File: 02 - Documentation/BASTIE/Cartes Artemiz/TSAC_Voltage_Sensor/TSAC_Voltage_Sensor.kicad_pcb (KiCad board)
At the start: 2 copper layers, 61 x 68.6 mm, 21 parts, among them J1 3P Droit 22-11-2032, K1 SSR CPC1394GR

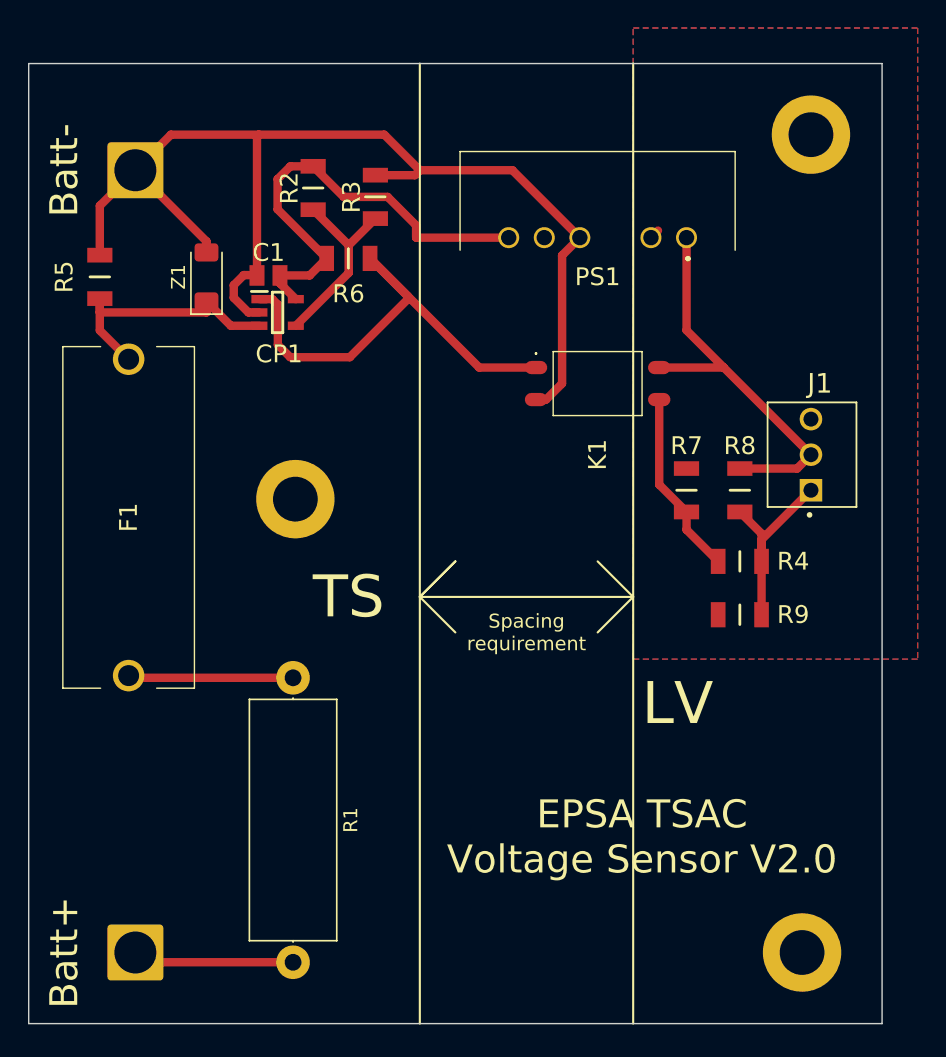
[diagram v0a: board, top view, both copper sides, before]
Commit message: Quasi fin modele 3D batterie + modif TSAC Voltage
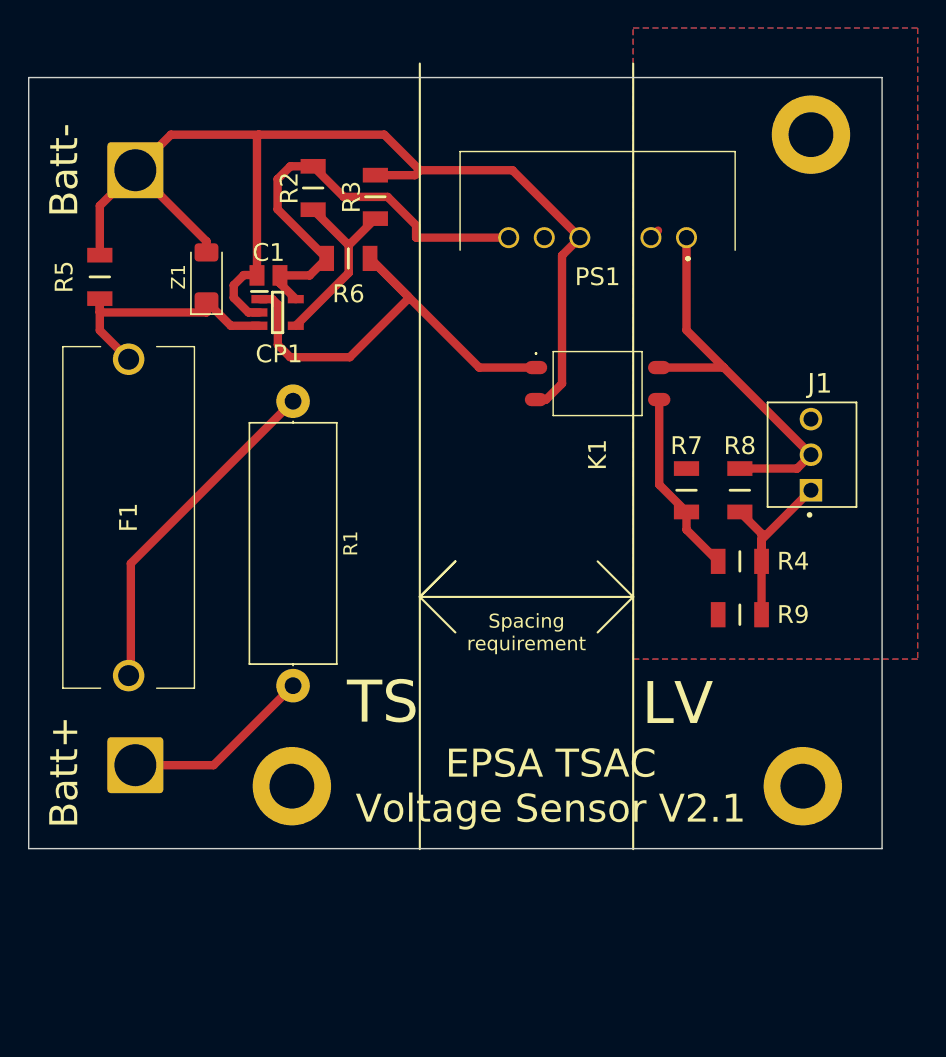
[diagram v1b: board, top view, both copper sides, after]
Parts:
- moved ? 20.5 mm to (95.0, 107.5)
- moved R1 19.8 mm to (95.1, 80.0)
- moved TP1 13.4 mm to (83.8, 106.0)
- moved ? 11.9 mm to (131.5, 107.5)
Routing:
- net Net-(F1-Pad1): track 11.6 -> 24.6 mm
- net +BATT: track 10.6 -> 13.6 mm
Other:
- board size 61 x 68.6 mm -> 61 x 55.1 mm
- board text added: "EPSA TSAC Voltage Sensor V2.1"
- board text removed: "EPSA TSAC Voltage Sensor V2.0"
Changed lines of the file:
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@@
 	(footprint ""
 		(layer "F.Cu")
-		(at 95.25 86.995)
+		(at 95 107.5)
 		(property "Reference" ""
 			(at 0 0 0)
@@
 	(footprint ""
 		(layer "F.Cu")
-		(at 131.445 119.38)
+		(at 131.5 107.5)
 		(property "Reference" ""
 			(at 0 0 0)
@@
 	(footprint "Connector_Wire:SolderWire-2.5sqmm_1x01_D2.4mm_OD3.6mm"
 		(layer "F.Cu")
-		(at 83.82 119.38)
+		(at 83.82 106)
 		(descr "Soldered wire connection, for a single 2.5 mm² wire, basic insulation, conductor diameter 2.4mm, outer diameter 3.6mm, size source Multi-Contact FLEXI-E 2.5 (https://ec.staubli.com/AcroFiles/Catalogues/TM_Cab-Main-11014119_(en)_hi.pdf), bend radius 3 times outer diameter, generated with kicad-footprint-generator")
 		(tags "connector wire 2.5sqmm")
@@
 	(footprint "Resistor_THT:R_Axial_DIN0617_L17.0mm_D6.0mm_P20.32mm_Horizontal"
 		(layer "F.Cu")
-		(at 95.085306 99.757822 -90)
+		(at 95.085306 80 -90)
 		(descr "Resistor, Axial_DIN0617 series, Axial, Horizontal, pin pitch=20.32mm, 2W, length*diameter=17*6mm^2, http://www.vishay.com/docs/20128/wkxwrx.pdf")
 		(tags "Resistor Axial_DIN0617 series Axial Horizontal pin pitch 20.32mm 2W length 17mm diameter 6mm")
 		(property "Reference" "R1"
-			(at 10.16 -4.12 -90)
+			(at 10.16 -4.12 90)
 			(layer "F.SilkS")
 			(effects
@@
 		)
 		(property "Value" "820k"
-			(at 10.16 4.12 -90)
+			(at 10.16 4.12 90)
 			(layer "F.Fab")
 			(effects
@@
 		)
 		(property "Description" "Thick Film Resistors - SMD"
-			(at 95.085306 99.757822 0)
+			(at 95.085306 99.757822 180)
 			(layer "F.Fab")
 			(hide yes)
@@
 		)
 		(property "Arrow Part Number" ""
-			(at 0 0 0)
+			(at 0 0 180)
 			(layer "F.Fab")
 			(hide yes)
@@
 		)
 		(property "Arrow Price/Stock" ""
-			(at 0 0 0)
+			(at 0 0 180)
 			(layer "F.Fab")
 			(hide yes)
@@
 		)
 		(property "Height" "0.7"
-			(at 0 0 0)
+			(at 0 0 180)
 			(layer "F.Fab")
 			(hide yes)
@@
 		)
 		(property "Manufacturer_Name" "KOA Speer"
-			(at 0 0 0)
+			(at 0 0 180)
 			(layer "F.Fab")
 			(hide yes)
@@
 		)
 		(property "Manufacturer_Part_Number" "RK73H2BLTDD2152F"
-			(at 0 0 0)
+			(at 0 0 180)
 			(layer "F.Fab")
 			(hide yes)
@@
 		)
 		(property "Mouser Part Number" "N/A"
-			(at 0 0 0)
+			(at 0 0 180)
 			(layer "F.Fab")
 			(hide yes)
@@
 		)
 		(property "Mouser Price/Stock" "https://www.mouser.co.uk/ProductDetail/KOA-Speer/RK73H2BLTDD2152F?qs=WeIALVmW3zmyxMFsjVzMRw%3D%3D"
-			(at 0 0 0)
+			(at 0 0 180)
 			(layer "F.Fab")
 			(hide yes)
@@
 		)
 		(property "Mouser Testing Part Number" ""
-			(at 0 0 0)
+			(at 0 0 180)
 			(layer "F.Fab")
 			(hide yes)
@@
 		)
 		(property "Mouser Testing Price/Stock" ""
-			(at 0 0 0)
+			(at 0 0 180)
 			(layer "F.Fab")
 			(hide yes)
@@
 		)
 		(property "Render Name" "Résistance"
-			(at 0 0 0)
+			(at 0 0 180)
 			(layer "F.Fab")
 			(hide yes)
@@
 		)
 		(fp_text user "${REFERENCE}"
-			(at 10.16 0 -90)
+			(at 10.16 0 90)
 			(layer "F.Fab")
 			(effects
@@
 	(gr_line
 		(start 119.38 55.88)
-		(end 119.38 124.46)
+		(end 119.38 112)
 		(stroke
 			(width 0.15)
@@
 	(gr_line
 		(start 104.14 55.88)
-		(end 104.14 124.46)
+		(end 104.14 112)
 		(stroke
 			(width 0.15)
@@
 	)
 	(gr_rect
-		(start 76.2 55.88)
-		(end 137.16 124.46)
+		(start 76.2 56.88)
+		(end 137.16 111.96)
 		(stroke
 			(width 0.1)
@@
 	)
 	(gr_text "Batt+"
-		(at 78.74 119.38 90)
+		(at 78.74 106.5 90)
 		(layer "F.SilkS")
 		(effects
@@
 	)
 	(gr_text "TS"
-		(at 99.06 93.98 0)
+		(at 101.5 101.5 0)
 		(layer "F.SilkS")
 		(effects
@@
 		)
 	)
-	(gr_text "EPSA TSAC\nVoltage Sensor V2.0"
-		(at 120.015 111.125 0)
+	(gr_text "EPSA TSAC\nVoltage Sensor V2.1"
+		(at 113.5 107.5 0)
 		(layer "F.SilkS")
 		(effects
@@
 	)
 	(segment
-		(start 84.517822 120.077822)
-		(end 95.085306 120.077822)
+		(start 89.405306 106)
+		(end 95.085306 100.32)
+		(width 0.6)
+		(layer "F.Cu")
+		(net 7)
+	)
+	(segment
+		(start 83.82 106)
+		(end 89.405306 106)
 		(width 0.6)
 		(layer "F.Cu")
@@
 	)
 	(segment
-		(start 95.085306 99.757822)
+		(start 83.496054 91.589252)
 		(end 83.496054 99.757822)
 		(width 0.6)
 		(layer "F.Cu")
+		(net 8)
+	)
+	(segment
+		(start 95.085306 80)
+		(end 83.496054 91.589252)
+		(width 0.6)
+		(layer "F.Cu")
